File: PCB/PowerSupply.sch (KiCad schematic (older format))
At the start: 21 parts, among them U2 MPM54304

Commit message: Cleaned up the schematics
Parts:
- U2: value MPM54304 -> MPM54304GMN-0001
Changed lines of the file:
@@
 AR Path="/60624089/60487643" Ref="U?"  Part="1"
 F 0 "U2" H 5750 6381 50  0000 C CNN
-F 1 "MPM54304" H 5750 3850 100 0000 C CNN
+F 1 "MPM54304GMN-0001" H 5750 3850 100 0000 C CNN
 F 2 "LitterRobot:MPS_MPM54304_LGA33_7x7mm" H 6300 6200 50  0001 C CNN
 F 3 "https://www.monolithicpower.com/en/documentview/productdocument/index/version/2/document_type/Datasheet/lang/en/sku/MPM54304/document_id/4982/" H 6300 6200 50  0001 C CNN

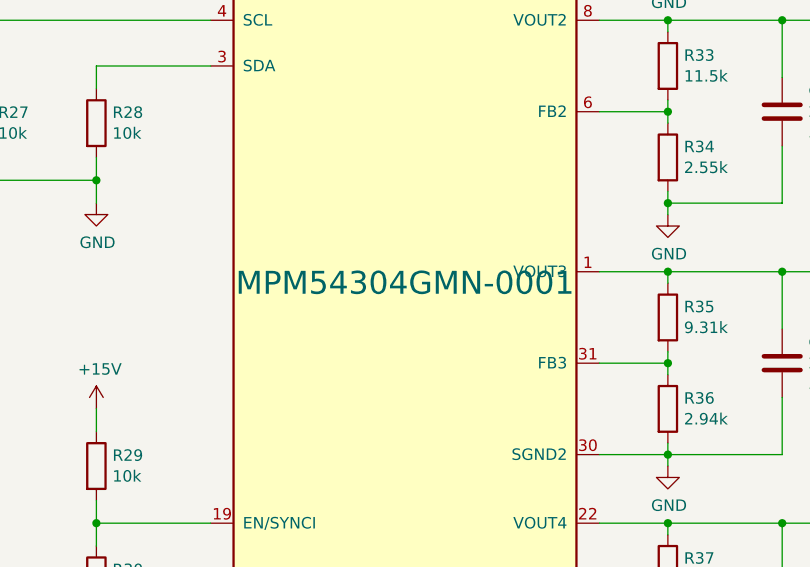
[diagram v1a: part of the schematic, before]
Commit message: Plot the schematic as PDF
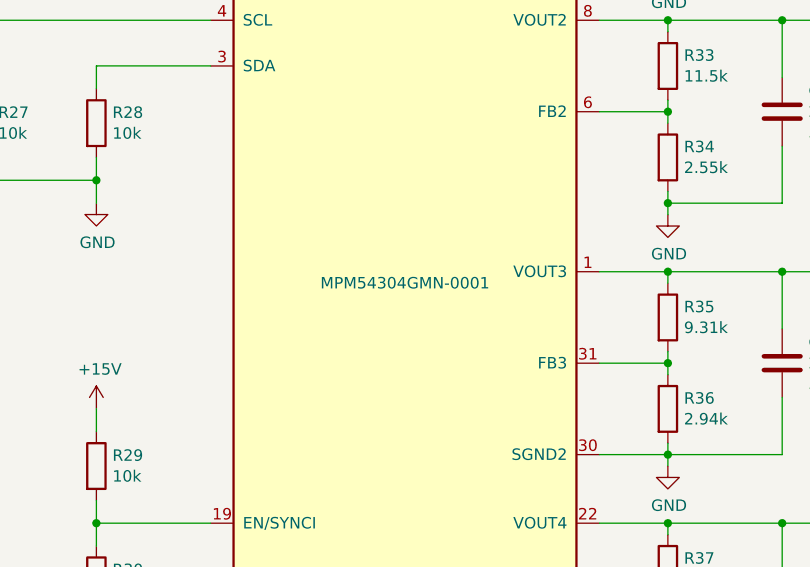
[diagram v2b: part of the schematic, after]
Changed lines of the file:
@@
 Sheet 15 19
 Title "Litter Robot 3 - Power supply"
-Date "2021-03-02"
+Date "2021-03-28"
 Rev "A1"
 Comp "L. Sartory"
@@
 AR Path="/60624089/60487643" Ref="U?"  Part="1"
 F 0 "U2" H 5750 6381 50  0000 C CNN
-F 1 "MPM54304GMN-0001" H 5750 3850 100 0000 C CNN
+F 1 "MPM54304GMN-0001" H 5750 3850 50  0000 C CNN
 F 2 "LitterRobot:MPS_MPM54304_LGA33_7x7mm" H 6300 6200 50  0001 C CNN
 F 3 "https://www.monolithicpower.com/en/documentview/productdocument/index/version/2/document_type/Datasheet/lang/en/sku/MPM54304/document_id/4982/" H 6300 6200 50  0001 C CNN

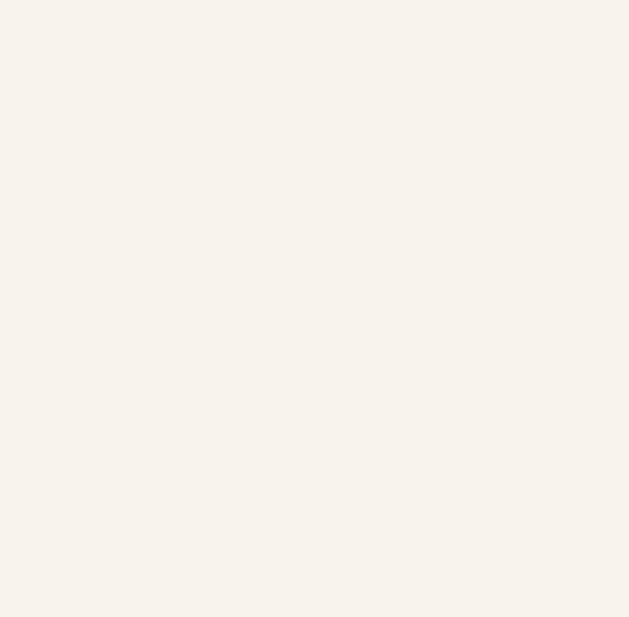
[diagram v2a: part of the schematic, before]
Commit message: Add reverse polarity protection diodes
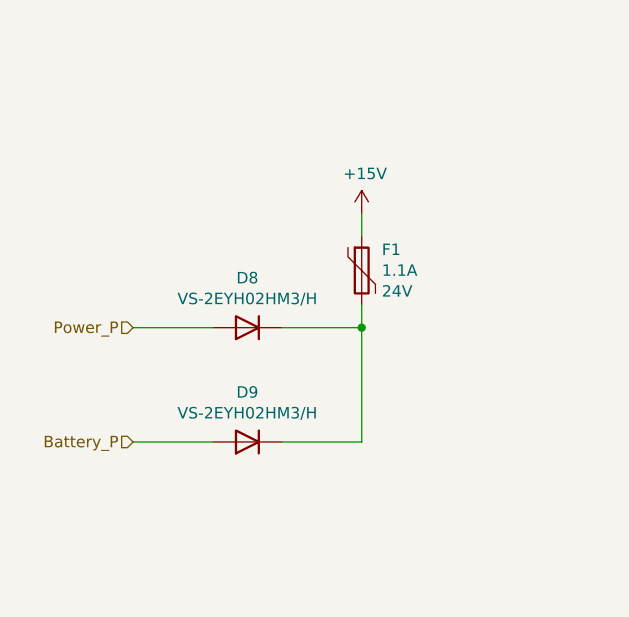
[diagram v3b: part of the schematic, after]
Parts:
- added D8, D9: VS-2EYH02HM3/H, Diode_SMD:D_SOD-128, symbol Device:D
- added F1: 1.1A, LitterRobot:Bel_Fuse_0ZCG, symbol Device:Polyfuse
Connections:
- net +15V: now also F1.1
- new net: D8.1 (K), D9.1 (K), F1.2
- new net Battery_P: D9.2 (A)
- new net Power_P: D8.2 (A)
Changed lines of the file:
@@
 Text Notes 6700 6250 0    50   ~ 0
 The pull-up resistor for the power-good signal is on the FPGA config page.
+Text HLabel 1500 4000 0    50   Input ~ 0
+Power_P
+Text HLabel 1500 4500 0    50   Input ~ 0
+Battery_P
+$Comp
+L Device:Polyfuse F?
+U 1 1 60688818
+P 2500 3750
+AR Path="/60688818" Ref="F?"  Part="1"
+AR Path="/603F1DCE/60688818" Ref="F1"  Part="1"
+F 0 "F1" H 2588 3841 50  0000 L CNN
+F 1 "1.1A" H 2588 3750 50  0000 L CNN
+F 2 "LitterRobot:Bel_Fuse_0ZCG" H 2550 3550 50  0001 L CNN
+F 3 "https://www.belfuse.com/resources/datasheets/circuitprotection/ds-cp-0zcg-series.pdf" H 2500 3750 50  0001 C CNN
+F 4 "0ZCG0110BF2B" H 2500 3750 50  0001 C CNN "Part_number"
+F 5 "24V" H 2588 3659 50  0000 L CNN "Voltage"
+	1    2500 3750
+	1    0    0    -1
+$EndComp
+$Comp
+L power:+15V #PWR?
+U 1 1 6068D8DA
+P 2500 3500
+AR Path="/6068D8DA" Ref="#PWR?"  Part="1"
+AR Path="/603F1DCE/6068D8DA" Ref="#PWR01"  Part="1"
+F 0 "#PWR01" H 2500 3350 50  0001 C CNN
+F 1 "+15V" H 2515 3673 50  0000 C CNN
+F 2 "" H 2500 3500 50  0001 C CNN
+F 3 "" H 2500 3500 50  0001 C CNN
+	1    2500 3500
+	1    0    0    -1
+$EndComp
+Wire Wire Line
+	2500 3500 2500 3600
+Wire Wire Line
+	2500 4000 2500 3900
+Connection ~ 2500 4000
+Wire Wire Line
+	1500 4000 1850 4000
+Wire Wire Line
+	2500 4500 2150 4500
+Wire Wire Line
+	2500 4000 2500 4500
+$Comp
+L Device:D D8
+U 1 1 606ADEF8
+P 2000 4000
+F 0 "D8" H 2000 3783 50  0000 C CNN
+F 1 "VS-2EYH02HM3/H" H 2000 3874 50  0000 C CNN
+F 2 "Diode_SMD:D_SOD-128" H 2000 4000 50  0001 C CNN
+F 3 "https://www.vishay.com/docs/96383/vs-2eyh02hm3.pdf" H 2000 4000 50  0001 C CNN
+F 4 "VS-2EYH02HM3/H" H 2000 4000 50  0001 C CNN "Part_number"
+	1    2000 4000
+	-1   0    0    1
+$EndComp
+Wire Wire Line
+	2150 4000 2500 4000
+$Comp
+L Device:D D9
+U 1 1 606AEF8E
+P 2000 4500
+F 0 "D9" H 2000 4283 50  0000 C CNN
+F 1 "VS-2EYH02HM3/H" H 2000 4374 50  0000 C CNN
+F 2 "Diode_SMD:D_SOD-128" H 2000 4500 50  0001 C CNN
+F 3 "https://www.vishay.com/docs/96383/vs-2eyh02hm3.pdf" H 2000 4500 50  0001 C CNN
+F 4 "VS-2EYH02HM3/H" H 2000 4500 50  0001 C CNN "Part_number"
+	1    2000 4500
+	-1   0    0    1
+$EndComp
+Wire Wire Line
+	1850 4500 1500 4500
 $EndSCHEMATC

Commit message: Add support for the weight sensor
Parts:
- renumbered R27 to R29, R28 to R30, R29 to R31, R30 to R32, R31 to R33, R32 to R34, R33 to R35, R34 to R36, R35 to R37, R36 to R38, R37 to R39, R38 to R40

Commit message: Re-annotate all components
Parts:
- renumbered C4 to C1, C5 to C2, C7 to C3, C8 to C4, C9 to C5, C10 to C6, C6 to C7, D8 to D1, D9 to D2, R38 to R10, R31 to R11, R39 to R12, R32 to R13, R40 to R14, R33 to R3, R34 to R4, R35 to R5, R29 to R6, R30 to R7, R36 to R8, R37 to R9, U2 to U1

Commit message: Change the higher value capacitors to 1206
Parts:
- C1, C2, C3, C4, C5, C6: footprint Capacitor_SMD:C_0603_1608Metric -> Capacitor_SMD:C_1206_3216Metric
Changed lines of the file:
@@
 F 0 "C2" H 4515 1941 50  0000 L CNN
 F 1 "22µF" H 4515 1850 50  0000 L CNN
-F 2 "Capacitor_SMD:C_0603_1608Metric" H 4438 1700 50  0001 C CNN
+F 2 "Capacitor_SMD:C_1206_3216Metric" H 4438 1700 50  0001 C CNN
 F 3 "https://product.tdk.com/system/files/dam/doc/product/capacitor/ceramic/mlcc/catalog/mlcc_commercial_general_en.pdf" H 4400 1850 50  0001 C CNN
 F 4 "35V" H 4515 1759 50  0000 L CNN "Voltage"
@@
 F 0 "C1" H 4015 1941 50  0000 L CNN
 F 1 "22µF" H 4015 1850 50  0000 L CNN
-F 2 "Capacitor_SMD:C_0603_1608Metric" H 3938 1700 50  0001 C CNN
+F 2 "Capacitor_SMD:C_1206_3216Metric" H 3938 1700 50  0001 C CNN
 F 3 "https://product.tdk.com/system/files/dam/doc/product/capacitor/ceramic/mlcc/catalog/mlcc_commercial_general_en.pdf" H 3900 1850 50  0001 C CNN
 F 4 "35V" H 4015 1759 50  0000 L CNN "Voltage"
@@
 F 0 "C3" H 7515 2091 50  0000 L CNN
 F 1 "22µF" H 7515 2000 50  0000 L CNN
-F 2 "Capacitor_SMD:C_0603_1608Metric" H 7438 1850 50  0001 C CNN
+F 2 "Capacitor_SMD:C_1206_3216Metric" H 7438 1850 50  0001 C CNN
 F 3 "https://product.tdk.com/system/files/dam/doc/product/capacitor/ceramic/mlcc/catalog/mlcc_commercial_general_en.pdf" H 7400 2000 50  0001 C CNN
 F 4 "35V" H 7515 1909 50  0000 L CNN "Voltage"
@@
 F 0 "C4" H 7515 3191 50  0000 L CNN
 F 1 "22µF" H 7515 3100 50  0000 L CNN
-F 2 "Capacitor_SMD:C_0603_1608Metric" H 7438 2950 50  0001 C CNN
+F 2 "Capacitor_SMD:C_1206_3216Metric" H 7438 2950 50  0001 C CNN
 F 3 "https://product.tdk.com/system/files/dam/doc/product/capacitor/ceramic/mlcc/catalog/mlcc_commercial_general_en.pdf" H 7400 3100 50  0001 C CNN
 F 4 "35V" H 7515 3009 50  0000 L CNN "Voltage"
@@
 F 0 "C5" H 7515 4291 50  0000 L CNN
 F 1 "22µF" H 7515 4200 50  0000 L CNN
-F 2 "Capacitor_SMD:C_0603_1608Metric" H 7438 4050 50  0001 C CNN
+F 2 "Capacitor_SMD:C_1206_3216Metric" H 7438 4050 50  0001 C CNN
 F 3 "https://product.tdk.com/system/files/dam/doc/product/capacitor/ceramic/mlcc/catalog/mlcc_commercial_general_en.pdf" H 7400 4200 50  0001 C CNN
 F 4 "35V" H 7515 4109 50  0000 L CNN "Voltage"
@@
 F 0 "C6" H 7515 5391 50  0000 L CNN
 F 1 "22µF" H 7515 5300 50  0000 L CNN
-F 2 "Capacitor_SMD:C_0603_1608Metric" H 7438 5150 50  0001 C CNN
+F 2 "Capacitor_SMD:C_1206_3216Metric" H 7438 5150 50  0001 C CNN
 F 3 "https://product.tdk.com/system/files/dam/doc/product/capacitor/ceramic/mlcc/catalog/mlcc_commercial_general_en.pdf" H 7400 5300 50  0001 C CNN
 F 4 "35V" H 7515 5209 50  0000 L CNN "Voltage"

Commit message: Add a 3D model for the SlimSMAW diodes
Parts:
- D1, D2: footprint Diode_SMD:D_SOD-128 -> LitterRobot:Vishay_SlimSMAW
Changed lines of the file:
@@
 F 0 "D1" H 2000 3783 50  0000 C CNN
 F 1 "VS-2EYH02HM3/H" H 2000 3874 50  0000 C CNN
-F 2 "Diode_SMD:D_SOD-128" H 2000 4000 50  0001 C CNN
+F 2 "LitterRobot:Vishay_SlimSMAW" H 2000 4000 50  0001 C CNN
 F 3 "https://www.vishay.com/docs/96383/vs-2eyh02hm3.pdf" H 2000 4000 50  0001 C CNN
 F 4 "VS-2EYH02HM3/H" H 2000 4000 50  0001 C CNN "Part_number"
@@
 F 0 "D2" H 2000 4283 50  0000 C CNN
 F 1 "VS-2EYH02HM3/H" H 2000 4374 50  0000 C CNN
-F 2 "Diode_SMD:D_SOD-128" H 2000 4500 50  0001 C CNN
+F 2 "LitterRobot:Vishay_SlimSMAW" H 2000 4500 50  0001 C CNN
 F 3 "https://www.vishay.com/docs/96383/vs-2eyh02hm3.pdf" H 2000 4500 50  0001 C CNN
 F 4 "VS-2EYH02HM3/H" H 2000 4500 50  0001 C CNN "Part_number"
